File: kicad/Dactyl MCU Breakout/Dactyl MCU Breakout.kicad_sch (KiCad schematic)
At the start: 19 parts, among them J1 Columns, J2 Rows, J3 Thumbs, J4 Display, J5 Split, J6 Extrernal, J7 JST, SW1 Reset, SW2 Battery, SW3 LED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

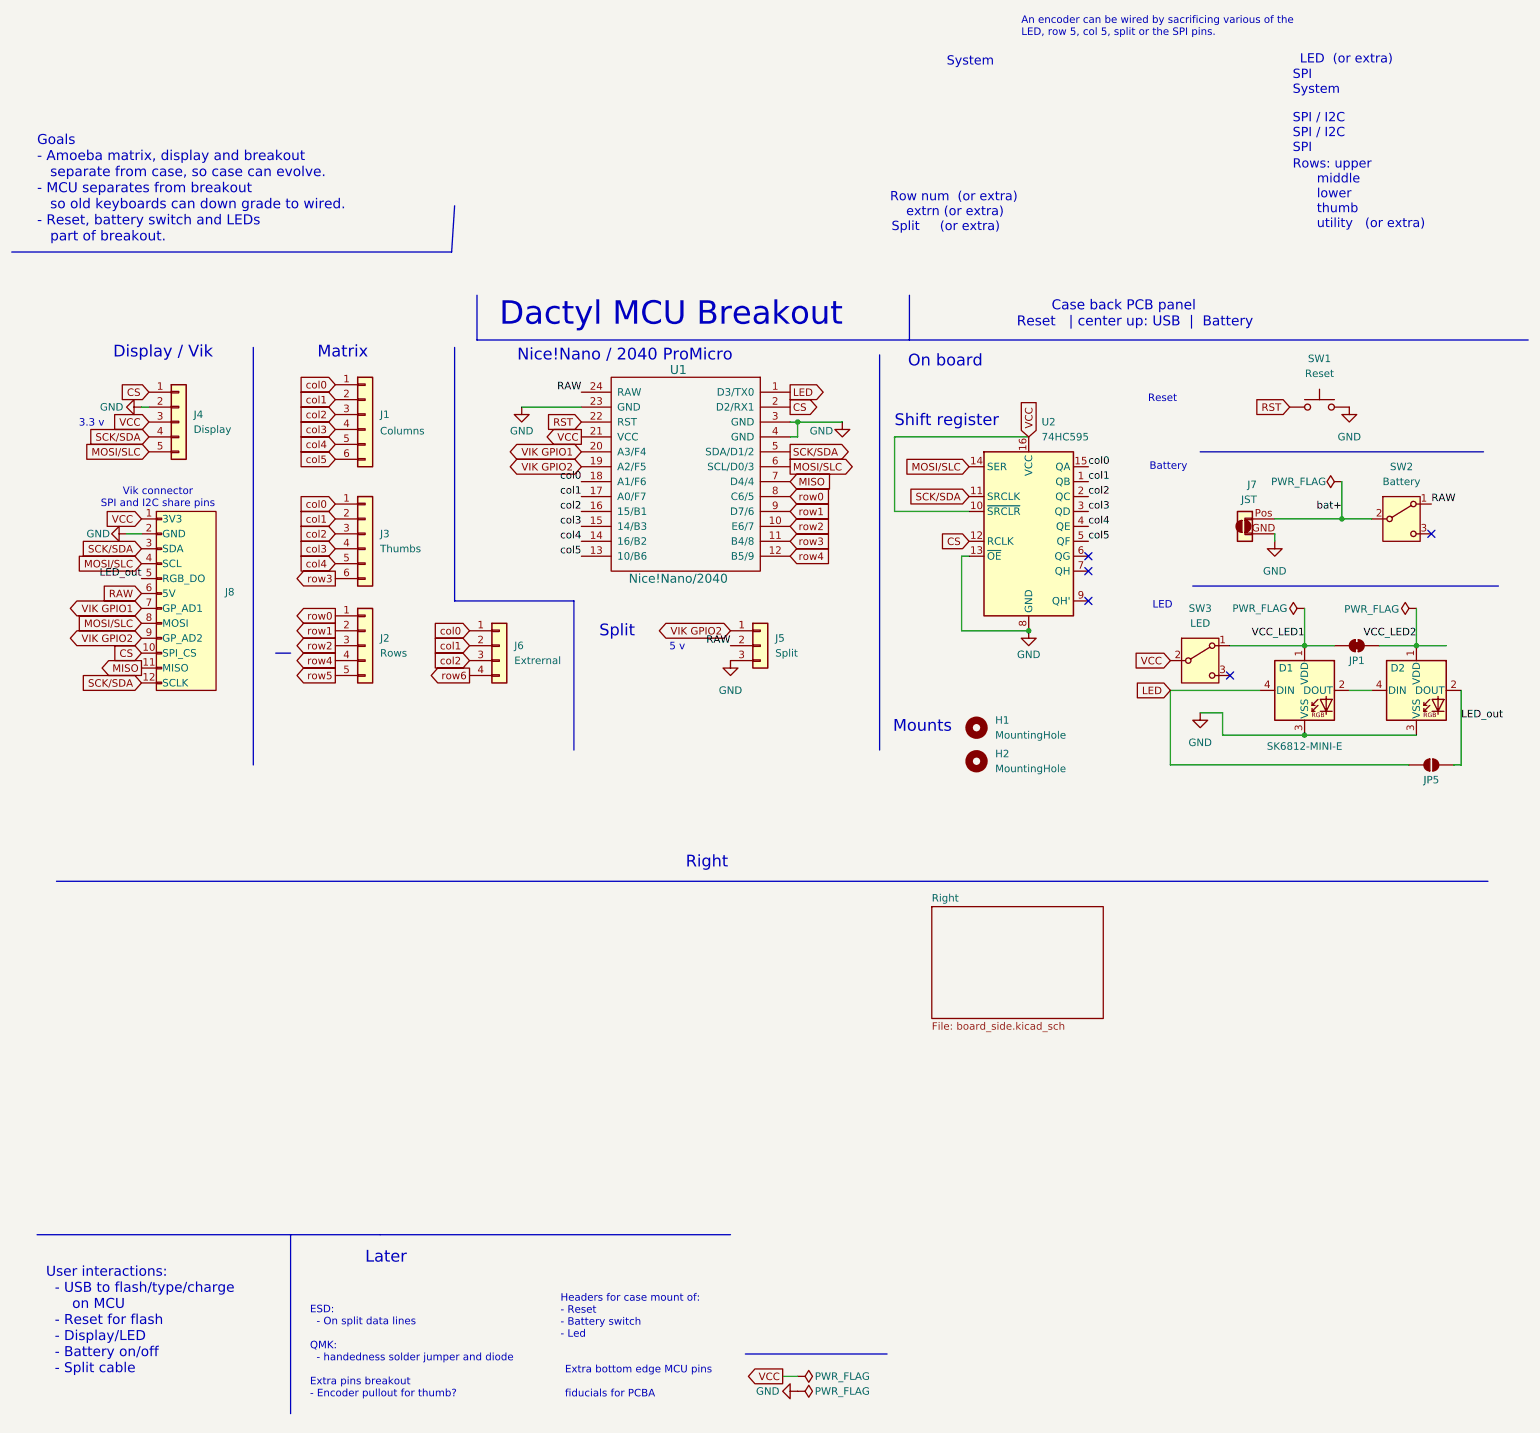
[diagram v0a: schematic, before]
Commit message: feat: bus SPI0, mum/2040 split steal form Vik
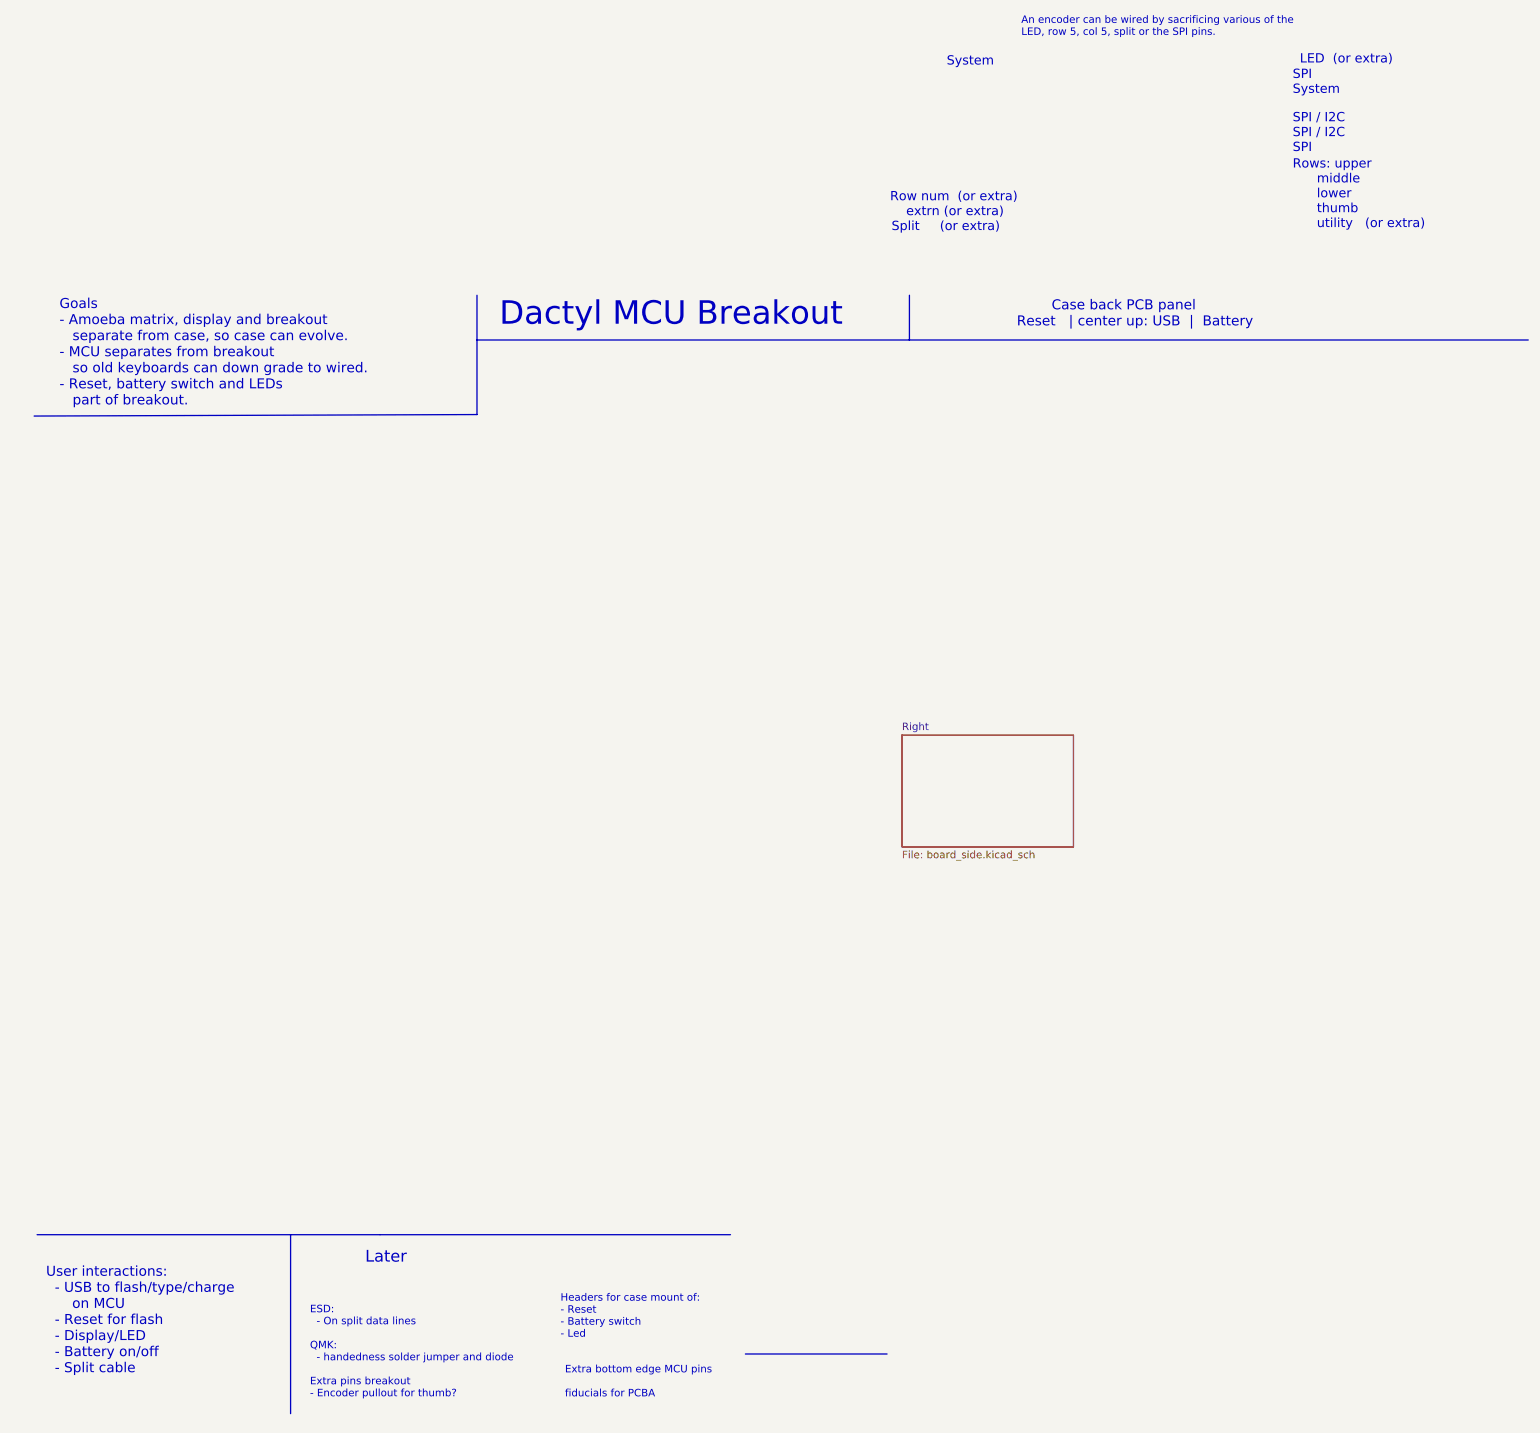
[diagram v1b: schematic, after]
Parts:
- removed D1, D2: SK6812-MINI-E, Dactyl:SK6812-MINI-E-Dog2, symbol Dactyl:SK6812-MINI-E
- removed H1, H2: MountingHole, MountingHole:MountingHole_3.2mm_M3_DIN965_Pad, symbol Mechanical:MountingHole
- removed J1: Columns, Connector_PinHeader_2.54mm:PinHeader_1x06_P2.54mm_Vertical, symbol Connector_Generic:Conn_01x06
- removed J2: Rows, Connector_PinHeader_2.54mm:PinHeader_1x05_P2.54mm_Vertical, symbol Connector_Generic:Conn_01x05
- removed J3: Thumbs, Connector_PinHeader_2.54mm:PinHeader_1x06_P2.54mm_Vertical, symbol Connector_Generic:Conn_01x06
- removed J4: Display, Connector_PinHeader_2.54mm:PinHeader_1x05_P2.54mm_Vertical, symbol Connector_Generic:Conn_01x05
- removed J5: Split, Connector_PinHeader_2.54mm:PinHeader_1x03_P2.54mm_Vertical, symbol Connector_Generic:Conn_01x03
- removed J6: Extrernal, Connector_PinHeader_2.54mm:PinHeader_1x04_P2.54mm_Vertical, symbol Connector_Generic:Conn_01x04
- removed J7: JST, Dactyl:JST_PH_S2B-PH-K_1x02_P2.00mm_Horizontal, symbol Dactyl:Conn_01x02_Jump_Two_Side
- removed J8: ~, symbol Dactyl:vik-keyboard-connector
- removed JP1: LED2 cutoff, Jumper:SolderJumper-2_P1.3mm_Bridged_RoundedPad1.0x1.5mm, symbol Jumper:SolderJumper_2_Bridged
- removed JP5: LED2 cutoff, Jumper:SolderJumper-2_P1.3mm_Bridged_RoundedPad1.0x1.5mm, symbol Jumper:SolderJumper_2_Open
- removed SW1: Reset, Dactyl:SW_Tactile_SKHL_Angled, symbol Switch:SW_Push
- removed SW2: Battery, Dactyl:SW_SPDT_JS202011AQN_wider, symbol Switch:SW_SPDT
- removed SW3: LED, Dactyl:SW_SPDT_JS202011AQN_wider, symbol Switch:SW_SPDT
- removed U1: Nice!Nano/2040, Dactyl:ProMicro_unrouted, symbol Dactyl:ProMicro_r
- removed U2: 74HC595, symbol 74xx:74HC595
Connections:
- no-connect marks 5 -> 0
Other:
- note removed: "3.3 v"
- note removed: "5 v"
- note removed: "Battery"
- note removed: "Display / Vik"
- note removed: "LED"
- note removed: "Matrix"
- note removed: "Mounts"
- note removed: "Nice!Nano / 2040 ProMicro"
- note removed: "On board"
- note removed: "Reset"
- note removed: "Right"
- note removed: "Shift register"
- note removed: "Split"
- note removed: "Vik connector SPI and I2C share pins"

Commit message: feat: add column to thumb, shift split to Vik AD1
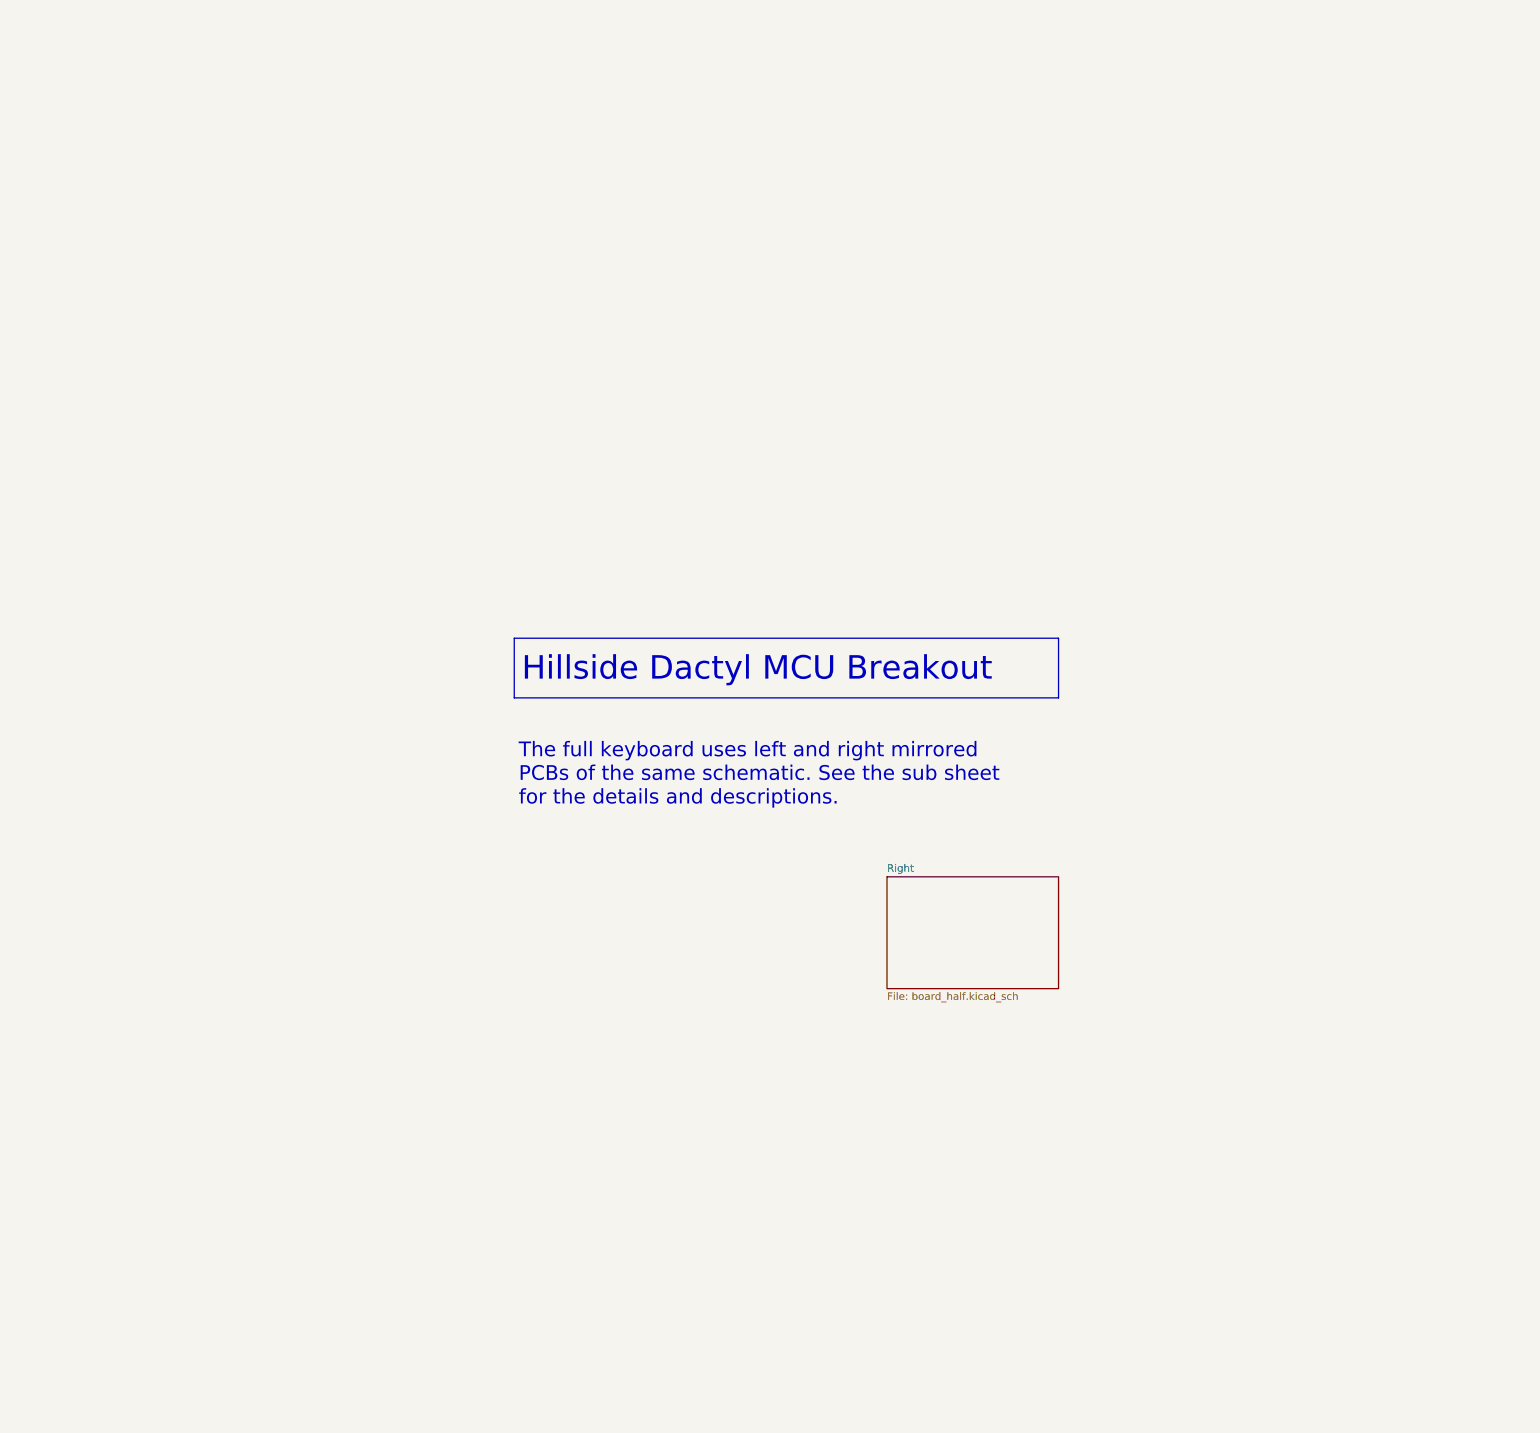
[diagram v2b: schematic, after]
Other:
- sheet Right: file board_side.kicad_sch -> board_half.kicad_sch
- note added: "The full keyboard uses left and right mirrored PCBs of the same schematic. See the sub sheet for the details and descriptions."
- note removed: "An encoder can be wired by sacrificing various of the LED, row 5, col 5, split or the SPI pins."
- note removed: "Case back PCB panel Reset | center up: USB | Battery"
- note removed: "ESD: - On split data lines QMK: - handedness solder jumper and diode Extra pins breakout - Encoder pullout for thumb?"
- note removed: "Extra bottom edge MCU pins fiducials for PCBA"
- note removed: "Goals - Amoeba matrix, display and breakout separate from case, so case can evolve. - MCU separates from breakout so old keyboards can down grade to wired. - Reset, battery switch and LEDs part of breakout."
- note removed: "Headers for case mount of: - Reset - Battery switch - Led"
- note removed: "LED (or extra)"
- note removed: "Later"
- note removed: "Row num (or extra) extrn (or extra)"
- note removed: "Rows: upper middle lower thumb utility (or extra)"
- note removed: "SPI"
- note removed: "SPI / I2C SPI / I2C SPI"
- note removed: "Split (or extra)"
- note removed: "System"
- note removed: "User interactions: - USB to flash/type/charge on MCU - Reset for flash - Display/LED - Battery on/off - Split cable"
- title: Dactyl MCU Breakout -> Hillside Dactyl MCU Breakout
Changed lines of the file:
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@@
 	(paper "USLetter")
 	(title_block
-		(title "Dactyl MCU Breakout")
+		(title "Hillside Dactyl MCU Breakout")
 		(date "2024-02-24")
 		(rev "0.1.0-alpha")
@@
 	(polyline
 		(pts
-			(xy 161.29 20.32) (xy 87.63 20.32)
+			(xy 93.98 71.12) (xy 186.69 71.12)
 		)
 		(stroke
@@
 	(polyline
 		(pts
-			(xy 266.7 20.32) (xy 161.29 20.32)
+			(xy 186.69 81.28) (xy 93.98 81.28)
 		)
 		(stroke
@@
 	(polyline
 		(pts
-			(xy 87.63 12.7) (xy 87.63 20.32)
+			(xy 93.98 71.12) (xy 93.98 81.28)
 		)
 		(stroke
@@
 	(polyline
 		(pts
-			(xy 12.7 172.72) (xy 71.12 172.72)
+			(xy 186.69 71.12) (xy 186.69 81.28)
 		)
 		(stroke
@@
 		)
 	)
-	(polyline
-		(pts
-			(xy 55.88 172.72) (xy 55.88 203.2)
-		)
-		(stroke
-			(width 0)
-			(type default)
-		)
-	)
-	(polyline
-		(pts
-			(xy 71.12 172.72) (xy 130.81 172.72)
-		)
-		(stroke
-			(width 0)
-			(type default)
-		)
-	)
-	(polyline
-		(pts
-			(xy 161.29 12.7) (xy 161.29 20.32)
-		)
-		(stroke
-			(width 0)
-			(type default)
-		)
-	)
-	(polyline
-		(pts
-			(xy 12.192 33.274) (xy 87.63 33.02)
-		)
-		(stroke
-			(width 0)
-			(type default)
-		)
-	)
-	(polyline
-		(pts
-			(xy 87.63 33.02) (xy 87.63 20.32)
-		)
-		(stroke
-			(width 0)
-			(type default)
-		)
-	)
-	(polyline
-		(pts
-			(xy 133.35 193.04) (xy 157.48 193.04)
-		)
-		(stroke
-			(width 0)
-			(type default)
-		)
-	)
-	(text "User interactions:\n  - USB to flash/type/charge\n      on MCU\n  - Reset for flash\n  - Display/LED\n  - Battery on/off\n  - Split cable\n"
-		(exclude_from_sim no)
-		(at 14.224 196.596 0)
-		(effects
-			(font
-				(size 1.7 1.7)
-			)
-			(justify left bottom)
-		)
-	)
-	(text "Rows: upper\n      middle\n      lower\n      thumb\n      utility   (or extra)"
-		(exclude_from_sim no)
-		(at 226.568 1.524 0)
-		(effects
-			(font
-				(size 1.5748 1.5748)
-			)
-			(justify left bottom)
-		)
-	)
-	(text "Later"
-		(exclude_from_sim no)
-		(at 68.58 177.8 0)
-		(effects
-			(font
-				(size 2 2)
-			)
-			(justify left bottom)
-		)
-	)
-	(text "Split     (or extra)\n"
-		(exclude_from_sim no)
-		(at 158.242 2.032 0)
-		(effects
-			(font
-				(size 1.5748 1.5748)
-			)
-			(justify left bottom)
-		)
-	)
-	(text "SPI / I2C\nSPI / I2C\nSPI"
-		(exclude_from_sim no)
-		(at 226.568 -11.43 0)
-		(effects
-			(font
-				(size 1.5748 1.5748)
-			)
-			(justify left bottom)
-		)
-	)
-	(text "Headers for case mount of:\n- Reset\n- Battery switch\n- Led"
-		(exclude_from_sim no)
-		(at 101.854 190.5 0)
-		(effects
-			(font
-				(size 1.27 1.27)
-			)
-			(justify left bottom)
-		)
-	)
-	(text "An encoder can be wired by sacrificing various of the \nLED, row 5, col 5, split or the SPI pins."
-		(exclude_from_sim no)
-		(at 180.34 -31.242 0)
-		(effects
-			(font
-				(size 1.27 1.27)
-			)
-			(justify left bottom)
-		)
-	)
 	(text "${TITLE}"
 		(exclude_from_sim no)
-		(at 91.44 18.288 0)
+		(at 95.25 78.74 0)
 		(effects
 			(font
@@
 		)
 	)
-	(text "Goals\n- Amoeba matrix, display and breakout  \n   separate from case, so case can evolve.\n- MCU separates from breakout \n   so old keyboards can down grade to wired.\n- Reset, battery switch and LEDs \n   part of breakout.\n"
+	(text "The full keyboard uses left and right mirrored  \nPCBs of the same schematic. See the sub sheet \nfor the details and descriptions."
 		(exclude_from_sim no)
-		(at 16.51 31.75 0)
+		(at 94.742 99.822 0)
 		(effects
 			(font
-				(size 1.7 1.7)
+				(size 2.5 2.5)
 			)
 			(justify left bottom)
 		)
 	)
-	(text "System"
-		(exclude_from_sim no)
-		(at 226.568 -21.336 0)
-		(effects
-			(font
-				(size 1.5748 1.5748)
-			)
-			(justify left bottom)
-		)
-	)
-	(text "        Case back PCB panel\nReset   | center up: USB  |  Battery\n"
-		(exclude_from_sim no)
-		(at 179.578 18.288 0)
-		(effects
-			(font
-				(size 1.7 1.7)
-			)
-			(justify left bottom)
-		)
-	)
-	(text "Extra bottom edge MCU pins\n\nfiducials for PCBA"
-		(exclude_from_sim no)
-		(at 102.616 200.66 0)
-		(effects
-			(font
-				(size 1.27 1.27)
-			)
-			(justify left bottom)
-		)
-	)
-	(text "SPI"
-		(exclude_from_sim no)
-		(at 226.568 -23.876 0)
-		(effects
-			(font
-				(size 1.5748 1.5748)
-			)
-			(justify left bottom)
-		)
-	)
-	(text "Row num  (or extra)\n    extrn (or extra)"
-		(exclude_from_sim no)
-		(at 157.988 -0.508 0)
-		(effects
-			(font
-				(size 1.5748 1.5748)
-			)
-			(justify left bottom)
-		)
-	)
-	(text "ESD: \n  - On split data lines\n\nQMK:\n  - handedness solder jumper and diode\n\nExtra pins breakout\n- Encoder pullout for thumb?\n\n"
-		(exclude_from_sim no)
-		(at 59.182 202.692 0)
-		(effects
-			(font
-				(size 1.27 1.27)
-			)
-			(justify left bottom)
-		)
-	)
-	(text "System"
-		(exclude_from_sim no)
-		(at 167.64 -26.162 0)
-		(effects
-			(font
-				(size 1.5748 1.5748)
-			)
-			(justify left bottom)
-		)
-	)
-	(text "LED  (or extra)"
-		(exclude_from_sim no)
-		(at 235.712 -27.432 0)
-		(effects
-			(font
-				(size 1.5748 1.5748)
-			)
-		)
-	)
 	(sheet
-		(at 160.02 87.63)
+		(at 157.48 111.76)
 		(size 29.21 19.05)
 		(fields_autoplaced yes)
@@
 		)
 		(property "Sheetname" "Right"
-			(at 160.02 86.9184 0)
+			(at 157.48 111.0484 0)
 			(effects
 				(font
@@
 			)
 		)
-		(property "Sheetfile" "board_side.kicad_sch"
-			(at 160.02 107.2646 0)
+		(property "Sheetfile" "board_half.kicad_sch"
+			(at 157.48 131.3946 0)
 			(effects
 				(font
